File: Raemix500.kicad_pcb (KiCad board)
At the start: 2 copper layers, 366 x 254 mm, 349 parts, among them CN1 LEFT_JOY, CN10 COMPOSITE, CN11 INTERNAL_FLOPPY, CN12 FLOPPY_POWER, CN13 KEYBOARD, CN14 IDE_POWER, CN15 IDE_I/F, CN2 RIGHT_JOY, CN3 RIGHT, CN4 LEFT, CN5 EXTFLOPPY_DB23F, CN6 SERIAL_DB25M, CN7 PARALLEL_DB25F, CN8 Power_Conn, CN9 VIDEO_DB23M, P1 EXPANSION BUS, P9 TRAPDOOR, Q301 2N3906, Q321 MPF102, Q331 MPF102, Q501 2N3904, Q502 2N3906, Q503 2N3906, Q711 2N3904, U1 68000D, U10 74LS244, U11 74LS373, U12 74LS244, U13 74LS373, U14 LF347, U15 74LS157, U16 XX4256, U17 XX4256, U18 XX4256, U19 XX4256, U2 FAT_AGNUS_8375, U20 XX4256, U21 XX4256, U22 XX4256, U23 XX4256, U3 PAULA, U32 74LS139, U33 74LS258, U34 74LS373, U35 74LS244, U36 74LS05, U37 74LS32, U38 MC1488, U39 MC1489, U4 DENISE, U40 74LS245, U41 74LS245, U42 NE555, U5 GARY_5719, U6 ROM, U7 VIA_8520, U8 VIA_8520, U9 MSM6242B, X1 XTAL, Y9 32768 Hz

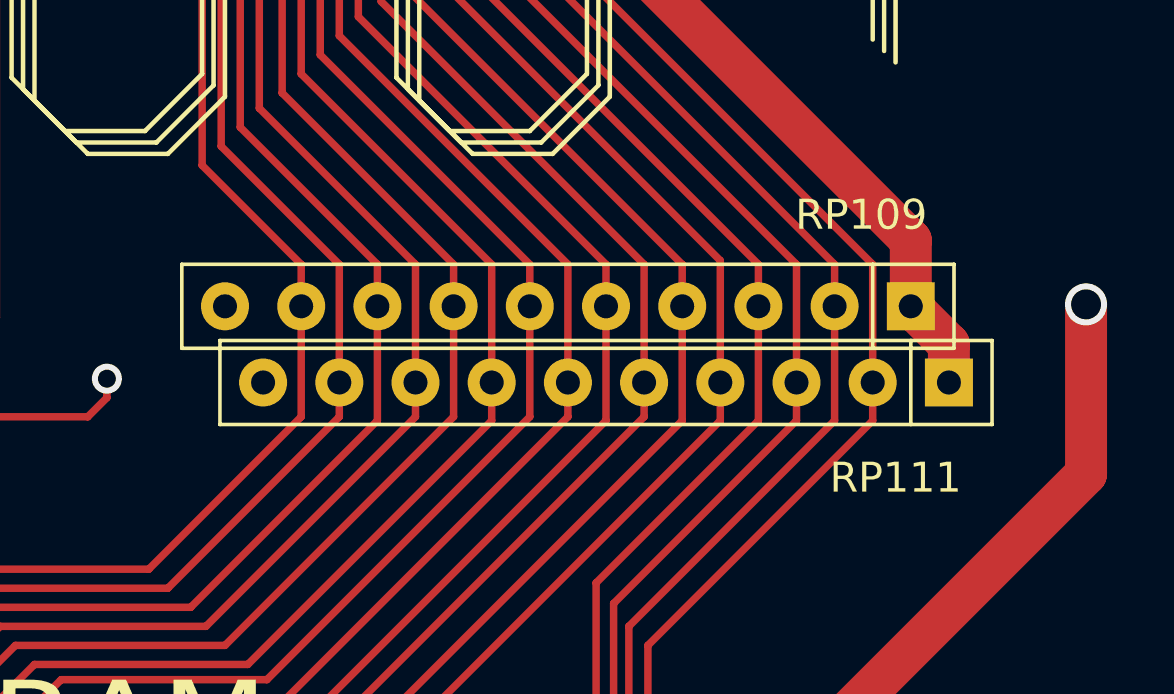
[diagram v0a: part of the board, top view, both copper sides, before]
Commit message: Place RP109/111 better
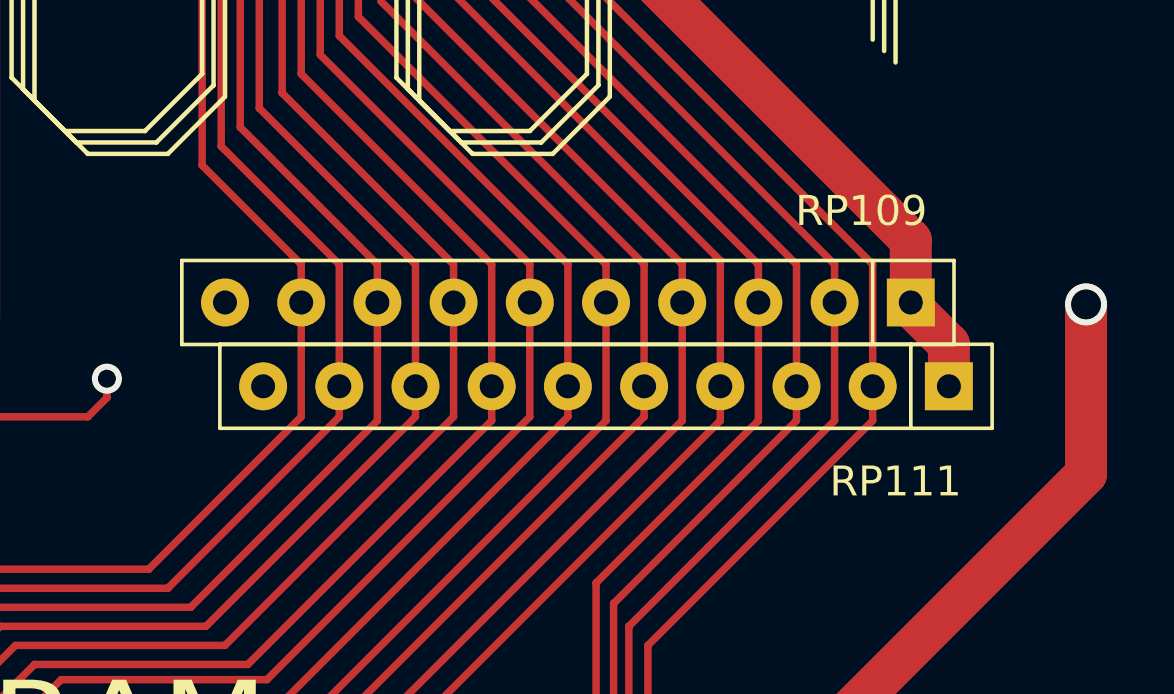
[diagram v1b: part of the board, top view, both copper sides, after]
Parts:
- moved RP109 0.13 mm to (184.0, 223.4)
- moved RP111 0.13 mm to (185.3, 226.2)
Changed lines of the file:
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@@
   )
   (module Resistor_THT:R_Array_SIP10 (layer F.Cu)
-    (at 184.023 223.52 180)
+    (at 184.023 223.393 180)
     (descr "10-pin Resistor SIP pack")
     (tags R)
@@
   )
   (module Resistor_THT:R_Array_SIP10 (layer F.Cu)
-    (at 185.293 226.06 180)
+    (at 185.293 226.187 180)
     (descr "10-pin Resistor SIP pack")
     (tags R)

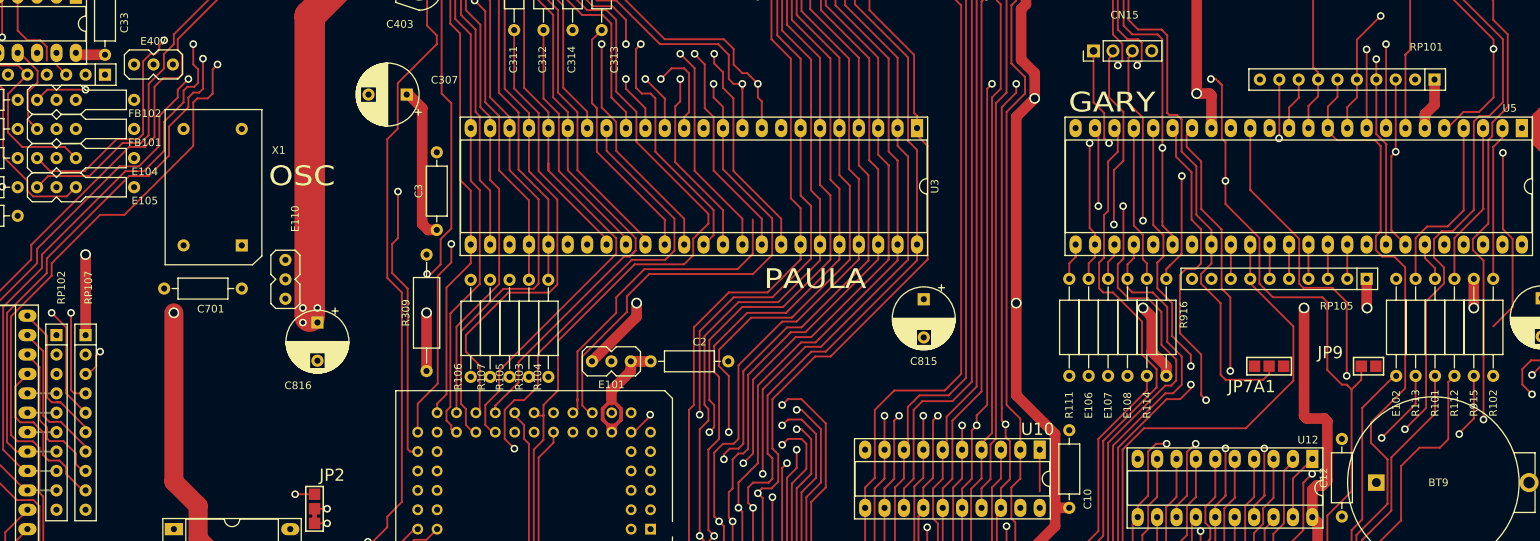
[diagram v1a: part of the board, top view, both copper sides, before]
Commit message: Add some tracks that got lost
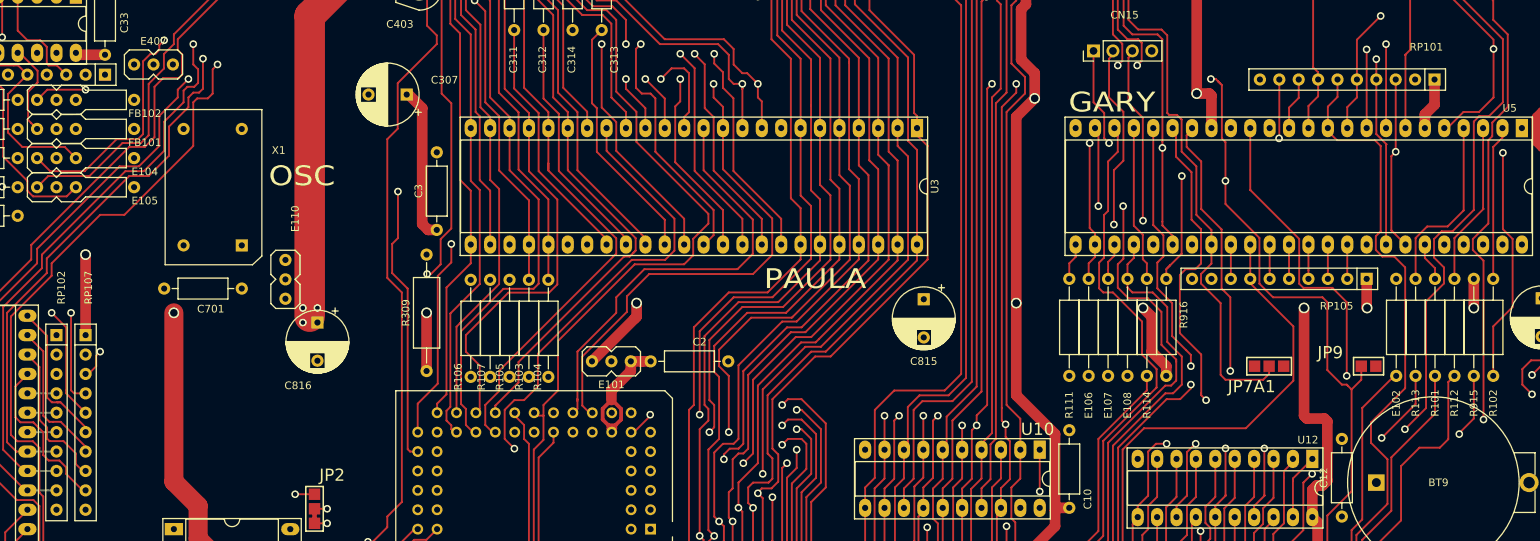
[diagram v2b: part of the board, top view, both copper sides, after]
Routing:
- net DMAL: track 42.5 -> 57.1 mm
- net ~VPA: track 111.5 -> 118.0 mm
- net Net-(RP103-Pad3): track 12.9 -> 14.7 mm
- net Net-(R113-Pad2): vias 1 -> 2
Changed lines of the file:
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@@
     (thickness 1.6)
     (drawings 315)
-    (tracks 5810)
+    (tracks 5816)
     (zones 0)
     (modules 349)
@@
     (solder_mask_min_width 0.25)
     (aux_axis_origin 29 24)
+    (grid_origin 160.909 123.317)
     (visible_elements FFFFF77F)
     (pcbplotparams
@@
   (segment (start 61.722 251.333) (end 65.532 247.523) (width 0.25) (layer F.Cu) (net 2))
   (segment (start 68.834 241.173) (end 68.834 201.349828) (width 0.25) (layer F.Cu) (net 2))
+  (segment (start 264.414 149.479) (end 264.414 155.956) (width 0.25) (layer F.Cu) (net 2))
   (segment (start 74.09791 177.84119) (end 72.9229 179.0162) (width 0.25) (layer F.Cu) (net 3) (status 20))
   (segment (start 74.09791 172.995295) (end 74.09791 177.84119) (width 0.25) (layer F.Cu) (net 3))
@@
   (segment (start 254.254 159.639) (end 249.809 164.084) (width 0.25) (layer F.Cu) (net 101))
   (segment (start 249.809 164.084) (end 249.682 164.084) (width 0.25) (layer F.Cu) (net 101))
+  (via (at 205.0474 171.0914) (size 1) (drill 0.6) (layers F.Cu B.Cu) (net 101))
   (segment (start 212.7944 198.0027) (end 212.7944 192.6814) (width 0.25) (layer F.Cu) (net 102) (status 10))
   (segment (start 212.7944 192.6814) (end 211.499 191.386) (width 0.25) (layer F.Cu) (net 102))
@@
   (segment (start 110.744 58.42) (end 110.744 54.61) (width 1.4) (layer F.Cu) (net 236))
   (segment (start 110.744 54.61) (end 110.744 52.649) (width 1.4) (layer F.Cu) (net 236) (status 20))
-  (segment (start 71.247 106.045) (end 71.247 110.744) (width 0.25) (layer F.Cu) (net 237) (status 10))
+  (segment (start 76.3905 115.316) (end 77.597 116.5225) (width 0.25) (layer F.Cu) (net 237))
+  (segment (start 75.311 115.316) (end 76.3905 115.316) (width 0.25) (layer F.Cu) (net 237))
   (segment (start 71.247 110.744) (end 72.517 112.014) (width 0.25) (layer F.Cu) (net 237))
-  (segment (start 74.197715 112.014) (end 75.057 112.873285) (width 0.25) (layer F.Cu) (net 237))
+  (segment (start 71.247 106.045) (end 71.247 110.744) (width 0.25) (layer F.Cu) (net 237))
+  (segment (start 75.057 112.873285) (end 75.057 115.062) (width 0.25) (layer F.Cu) (net 237))
   (segment (start 72.517 112.014) (end 74.197715 112.014) (width 0.25) (layer F.Cu) (net 237))
-  (segment (start 75.057 112.873285) (end 75.057 114.681) (width 0.25) (layer F.Cu) (net 237))
-  (segment (start 76.3905 115.316) (end 77.597 116.5225) (width 0.25) (layer F.Cu) (net 237) (status 20))
+  (segment (start 74.197715 112.014) (end 75.057 112.873285) (width 0.25) (layer F.Cu) (net 237))
+  (segment (start 75.057 115.062) (end 75.311 115.316) (width 0.25) (layer F.Cu) (net 237))
   (segment (start 103.759 57.785) (end 103.759 66.04) (width 0.25) (layer F.Cu) (net 238))
   (segment (start 87.249 57.15) (end 103.124 57.15) (width 0.25) (layer F.Cu) (net 238))
@@
   (segment (start 144.526 152.781) (end 144.526 159.004) (width 0.25) (layer F.Cu) (net 331))
   (segment (start 144.526 159.004) (end 144.526 159.258) (width 0.25) (layer F.Cu) (net 331))
+  (segment (start 161.0419 129.0379) (end 167.48689 135.48289) (width 0.25) (layer F.Cu) (net 331))
+  (segment (start 161.0419 123.5172) (end 161.0419 129.0379) (width 0.25) (layer F.Cu) (net 331))
   (segment (start 155.9619 138.7572) (end 155.9619 135.5149) (width 0.25) (layer F.Cu) (net 332) (status 10))
   (segment (start 155.9619 135.5149) (end 147.066 126.619) (width 0.25) (layer F.Cu) (net 332))
